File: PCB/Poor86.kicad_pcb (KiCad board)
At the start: 2 copper layers, 0 parts

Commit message: broken 386 symbol
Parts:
- added C10: 47uF, Capacitor_SMD:C_0603_1608Metric, F.Cu at (74.8, 82.2)
- added C5: 47uF, Capacitor_SMD:C_0603_1608Metric, F.Cu at (48.1, 113.2)
- added C6: 47uF, Capacitor_SMD:C_0603_1608Metric, F.Cu at (48.1, 115.7)
- added C7: 47uF, Capacitor_SMD:C_0603_1608Metric, F.Cu at (48.1, 118.2)
- added C8: 47uF, Capacitor_SMD:C_0603_1608Metric, F.Cu at (48.1, 120.7)
- added C9: 47uF, Capacitor_SMD:C_0603_1608Metric, F.Cu at (48.1, 123.2)
- added CDC1: 1uF, Capacitor_SMD:C_0402_1005Metric, F.Cu at (47.5, 97.1)
- added CDC10: 1uF, Capacitor_SMD:C_0402_1005Metric, F.Cu at (50.4, 99.1)
- added CDC11: 1uF, Capacitor_SMD:C_0402_1005Metric, F.Cu at (50.4, 101.1)
- added CDC12: 1uF, Capacitor_SMD:C_0402_1005Metric, F.Cu at (50.4, 103.0)
- added CDC13: 1uF, Capacitor_SMD:C_0402_1005Metric, F.Cu at (50.4, 105.0)
- added CDC14: 1uF, Capacitor_SMD:C_0402_1005Metric, F.Cu at (50.4, 107.0)
- added CDC15: 1uF, Capacitor_SMD:C_0402_1005Metric, F.Cu at (50.4, 109.0)
- added CDC16: 1uF, Capacitor_SMD:C_0402_1005Metric, F.Cu at (50.4, 110.9)
- added CDC17: 1uF, Capacitor_SMD:C_0402_1005Metric, F.Cu at (53.2, 97.1)
- added CDC18: 1uF, Capacitor_SMD:C_0402_1005Metric, F.Cu at (53.2, 99.1)
- added CDC19: 1uF, Capacitor_SMD:C_0402_1005Metric, F.Cu at (53.2, 101.1)
- added CDC2: 1uF, Capacitor_SMD:C_0402_1005Metric, F.Cu at (47.5, 99.1)
- added CDC20: 1uF, Capacitor_SMD:C_0402_1005Metric, F.Cu at (53.2, 103.0)
- added CDC21: 1uF, Capacitor_SMD:C_0402_1005Metric, F.Cu at (53.2, 105.0)
- added CDC22: 1uF, Capacitor_SMD:C_0402_1005Metric, F.Cu at (53.2, 107.0)
- added CDC23: 1uF, Capacitor_SMD:C_0402_1005Metric, F.Cu at (53.2, 109.0)
- added CDC24: 1uF, Capacitor_SMD:C_0402_1005Metric, F.Cu at (53.2, 110.9)
- added CDC25: 1uF, Capacitor_SMD:C_0402_1005Metric, F.Cu at (56.1, 97.1)
- added CDC26: 1uF, Capacitor_SMD:C_0402_1005Metric, F.Cu at (56.1, 99.1)
- added CDC27: 1uF, Capacitor_SMD:C_0402_1005Metric, F.Cu at (56.1, 101.1)
- added CDC28: 1uF, Capacitor_SMD:C_0402_1005Metric, F.Cu at (56.1, 103.0)
- added CDC29: 1uF, Capacitor_SMD:C_0402_1005Metric, F.Cu at (56.1, 105.0)
- added CDC3: 1uF, Capacitor_SMD:C_0402_1005Metric, F.Cu at (47.5, 101.1)
- added CDC30: 1uF, Capacitor_SMD:C_0402_1005Metric, F.Cu at (56.1, 107.0)
- added CDC31: 1uF, Capacitor_SMD:C_0402_1005Metric, F.Cu at (56.1, 109.0)
- added CDC32: 1uF, Capacitor_SMD:C_0402_1005Metric, F.Cu at (56.1, 110.9)
- added CDC33: 1uF, Capacitor_SMD:C_0402_1005Metric, F.Cu at (59.0, 97.1)
- added CDC34: 1uF, Capacitor_SMD:C_0402_1005Metric, F.Cu at (59.0, 99.1)
- added CDC35: 1uF, Capacitor_SMD:C_0402_1005Metric, F.Cu at (73.6, 58.6)
- added CDC36: 1uF, Capacitor_SMD:C_0402_1005Metric, F.Cu at (59.0, 103.0)
- added CDC37: 1uF, Capacitor_SMD:C_0402_1005Metric, F.Cu at (59.0, 105.0)
- added CDC38: 1uF, Capacitor_SMD:C_0402_1005Metric, F.Cu at (59.0, 107.0)
- added CDC4: 1uF, Capacitor_SMD:C_0402_1005Metric, F.Cu at (47.5, 103.0)
- added CDC5: 1uF, Capacitor_SMD:C_0402_1005Metric, F.Cu at (47.5, 105.0)
- added CDC6: 1uF, Capacitor_SMD:C_0402_1005Metric, F.Cu at (47.5, 107.0)
- added CDC7: 1uF, Capacitor_SMD:C_0402_1005Metric, F.Cu at (47.5, 109.0)
- added CDC8: 1uF, Capacitor_SMD:C_0402_1005Metric, F.Cu at (47.5, 110.9)
- added CDC9: 1uF, Capacitor_SMD:C_0402_1005Metric, F.Cu at (50.4, 97.1)
- added U3: ~, Package_QFP:LQFP-208_28x28mm_P0.5mm, F.Cu at (54.2, 70.1)

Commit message: ...
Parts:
- moved C6 57.6 mm to (99.2, 89.1)
- moved C7 57.6 mm to (99.2, 91.6)
- moved C8 57.6 mm to (99.2, 94.1)
- moved C9 57.6 mm to (99.2, 96.7)
- moved C5 51.6 mm to (71.4, 67.1), turned to 180 degrees
- moved C10 31.2 mm to (64.2, 52.8), turned to -90 degrees
- moved CDC35 2.92 mm to (70.8, 57.7), turned to 180 degrees
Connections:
- U3 pad 100: unconnected-(U3C-D19-Pad100) -> /am5x86/D19
- U3 pad 101: unconnected-(U3C-D18-Pad101) -> /am5x86/D18
- U3 pad 103: unconnected-(U3C-D17-Pad103) -> /am5x86/D17
- U3 pad 108: unconnected-(U3C-D16-Pad108) -> /am5x86/D16
- U3 pad 112: unconnected-(U3C-D15-Pad112) -> /am5x86/D15
- U3 pad 113: unconnected-(U3C-D14-Pad113) -> /am5x86/D14
- U3 pad 116: unconnected-(U3C-D13-Pad116) -> /am5x86/D13
- U3 pad 117: unconnected-(U3C-D12-Pad117) -> /am5x86/D12
- U3 pad 118: unconnected-(U3C-D11-Pad118) -> /am5x86/D11
- U3 pad 119: unconnected-(U3C-D10-Pad119) -> /am5x86/D10
- U3 pad 123: unconnected-(U3C-D9-Pad123) -> /am5x86/D9
- U3 pad 124: unconnected-(U3C-D8-Pad124) -> /am5x86/D8
- U3 pad 126: unconnected-(U3C-D7-Pad126) -> /am5x86/D7
- U3 pad 129: unconnected-(U3C-D6-Pad129) -> /am5x86/D6
- U3 pad 130: unconnected-(U3C-D5-Pad130) -> /am5x86/D5
- U3 pad 140: unconnected-(U3C-D4-Pad140) -> /am5x86/D4
- U3 pad 141: unconnected-(U3C-D3-Pad141) -> /am5x86/D3
- U3 pad 142: unconnected-(U3C-D2-Pad142) -> /am5x86/D2
- U3 pad 143: unconnected-(U3C-D1-Pad143) -> /am5x86/D1
- U3 pad 144: unconnected-(U3C-D0-Pad144) -> /am5x86/D0
- U3 pad 147: unconnected-(U3C-A31-Pad147) -> /am5x86/A31
- U3 pad 148: unconnected-(U3C-A30-Pad148) -> /am5x86/A30
- U3 pad 149: unconnected-(U3C-A29-Pad149) -> /am5x86/A29
- U3 pad 151: unconnected-(U3C-A28-Pad151) -> /am5x86/A28
- U3 pad 152: unconnected-(U3C-A27-Pad152) -> /am5x86/A27
- U3 pad 153: unconnected-(U3C-A26-Pad153) -> /am5x86/A26
- U3 pad 154: unconnected-(U3C-A25-Pad154) -> /am5x86/A25
- U3 pad 158: unconnected-(U3C-A24-Pad158) -> /am5x86/A24
- U3 pad 159: unconnected-(U3C-A23-Pad159) -> /am5x86/A23
- U3 pad 160: unconnected-(U3C-A22-Pad160) -> /am5x86/A22
- U3 pad 161: unconnected-(U3C-A21-Pad161) -> /am5x86/A21
- U3 pad 164: unconnected-(U3C-A20-Pad164) -> /am5x86/A20
- U3 pad 165: unconnected-(U3C-A19-Pad165) -> /am5x86/A19
- U3 pad 166: unconnected-(U3C-A18-Pad166) -> /am5x86/A18
- U3 pad 171: unconnected-(U3C-A17-Pad171) -> /am5x86/A17
- U3 pad 173: unconnected-(U3C-A16-Pad173) -> /am5x86/A16
- U3 pad 174: unconnected-(U3C-A15-Pad174) -> /am5x86/A15
- U3 pad 177: unconnected-(U3C-A14-Pad177) -> /am5x86/A14
- U3 pad 178: unconnected-(U3C-A13-Pad178) -> /am5x86/A13
- U3 pad 180: unconnected-(U3C-A12-Pad180) -> /am5x86/A12
- U3 pad 182: unconnected-(U3C-A11-Pad182) -> /am5x86/A11
- U3 pad 186: unconnected-(U3C-A10-Pad186) -> /am5x86/A10
- U3 pad 187: unconnected-(U3C-A9-Pad187) -> /am5x86/A9
- U3 pad 190: unconnected-(U3C-A8-Pad190) -> /am5x86/A8
- U3 pad 192: unconnected-(U3C-A7-Pad192) -> /am5x86/A7
- U3 pad 193: unconnected-(U3C-A6-Pad193) -> /am5x86/A6
- U3 pad 195: unconnected-(U3C-A5-Pad195) -> /am5x86/A5
- U3 pad 196: unconnected-(U3C-A4-Pad196) -> /am5x86/A4
- U3 pad 197: unconnected-(U3C-A3-Pad197) -> /am5x86/A3
- U3 pad 202: unconnected-(U3C-A2-Pad202) -> /am5x86/A2
- U3 pad 74: unconnected-(U3C-D31-Pad74) -> /am5x86/D31
- U3 pad 75: unconnected-(U3C-D30-Pad75) -> /am5x86/D30
- U3 pad 78: unconnected-(U3C-D29-Pad78) -> /am5x86/D29
- U3 pad 79: unconnected-(U3C-D28-Pad79) -> /am5x86/D28
- U3 pad 83: unconnected-(U3C-D27-Pad83) -> /am5x86/D27
- U3 pad 84: unconnected-(U3C-D26-Pad84) -> /am5x86/D26
- U3 pad 85: unconnected-(U3C-D25-Pad85) -> /am5x86/D25
- U3 pad 87: unconnected-(U3C-D24-Pad87) -> /am5x86/D24
- U3 pad 91: unconnected-(U3C-D23-Pad91) -> /am5x86/D23
- U3 pad 92: unconnected-(U3C-D22-Pad92) -> /am5x86/D22
- U3 pad 93: unconnected-(U3C-D21-Pad93) -> /am5x86/D21
- U3 pad 99: unconnected-(U3C-D20-Pad99) -> /am5x86/D20
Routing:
- net +3V3: track 0.00 -> 9.24 mm, vias 0 -> 5
- net GNDD: track 0.00 -> 2.85 mm, vias 0 -> 11
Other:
- copper layers 2 -> 4

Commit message: progress
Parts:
- added C1: 100pF, Capacitor_SMD:C_0402_1005Metric, F.Cu at (84.7, 96.4)
- added C11: 1u, Capacitor_SMD:C_0402_1005Metric, F.Cu at (99.4, 79.5)
- added C12: 1u, Capacitor_SMD:C_0402_1005Metric, F.Cu at (102.3, 71.7)
- added C13: 1u, Capacitor_SMD:C_0402_1005Metric, F.Cu at (102.3, 73.6)
- added C14: 47uF, Capacitor_SMD:C_0603_1608Metric, F.Cu at (96.0, 71.9)
- added C15: 47uF, Capacitor_SMD:C_0603_1608Metric, F.Cu at (96.0, 74.5)
- added C16: 100pF, Capacitor_SMD:C_0402_1005Metric, F.Cu at (87.5, 100.3)
- added C17: 1u, Capacitor_SMD:C_0402_1005Metric, F.Cu at (87.5, 102.3)
- added C18: 1u, Capacitor_SMD:C_0402_1005Metric, F.Cu at (87.5, 104.3)
- added C19: 1u, Capacitor_SMD:C_0402_1005Metric, F.Cu at (90.4, 96.4)
- added C2: 1u, Capacitor_SMD:C_0402_1005Metric, F.Cu at (99.4, 73.6)
- added C20: 1u, Capacitor_SMD:C_0402_1005Metric, F.Cu at (90.4, 98.3)
- added C21: 1u, Capacitor_SMD:C_0402_1005Metric, F.Cu at (90.4, 100.3)
- added C22: 1u, Capacitor_SMD:C_0402_1005Metric, F.Cu at (90.4, 102.3)
- added C23: 47uF, Capacitor_SMD:C_0603_1608Metric, F.Cu at (81.2, 101.7)
- added C24: 47uF, Capacitor_SMD:C_0603_1608Metric, F.Cu at (81.2, 104.2)
- added C3: 1u, Capacitor_SMD:C_0402_1005Metric, F.Cu at (99.4, 75.6)
- added C4: 1u, Capacitor_SMD:C_0402_1005Metric, F.Cu at (99.4, 77.6)
- added L1: 2.2uH, Inductor_SMD:L_1008_2520Metric, F.Cu at (113.3, 79.7)
- added L2: 2.2uH, Inductor_SMD:L_1008_2520Metric, F.Cu at (85.7, 110.9)
- added R1: 15k, Resistor_SMD:R_0402_1005Metric, F.Cu at (93.3, 96.4)
- added R2: 18k, Resistor_SMD:R_0402_1005Metric, F.Cu at (93.3, 98.4)
- added R3: 15k, Resistor_SMD:R_0402_1005Metric, F.Cu at (93.3, 100.4)
- added R4: 4.7K, Resistor_SMD:R_0402_1005Metric, F.Cu at (93.3, 102.4)
- added U1: LFE5U-25F-6BG256C, ECP5:BGA256C80P16X16_1400X1400X170, F.Cu at (51.2, 109.6)
- added U2: TLV62569DBV, Package_TO_SOT_SMD:SOT-23-5, F.Cu at (111.7, 86.3)
- added U4: TLV62569DBV, Package_TO_SOT_SMD:SOT-23-5, F.Cu at (73.5, 104.3)
- added U5: TLV62569DBV, Package_TO_SOT_SMD:SOT-23-5, F.Cu at (73.5, 108.9)
- CDC1, CDC10, CDC11, CDC12, CDC13, CDC14, CDC15, CDC16, CDC17, CDC18, CDC19, CDC2, CDC20, CDC21, CDC22, CDC23, CDC24, CDC25, CDC26, CDC27, CDC28, CDC29, CDC3, CDC30, CDC31, CDC32, CDC33, CDC34, CDC36, CDC37, CDC38, CDC4, CDC5, CDC6, CDC7, CDC8, CDC9: moved to B.Cu
- moved C8 68.0 mm to (37.0, 66.6)
- moved C6 65.7 mm to (37.0, 68.2)
- moved C9 64.7 mm to (37.0, 79.1)
- moved CDC16 46.5 mm to (52.2, 64.5)
- moved CDC24 46.5 mm to (55.0, 64.5)
- moved CDC32 46.5 mm to (57.9, 64.5)
- moved CDC8 46.5 mm to (49.3, 64.5)
- moved CDC15 42.5 mm to (52.2, 66.5)
- moved CDC23 42.5 mm to (55.0, 66.5)
- moved CDC31 42.5 mm to (57.9, 66.5)
- moved CDC7 42.5 mm to (49.3, 66.5)
- moved CDC14 38.6 mm to (52.2, 68.4)
- moved CDC22 38.6 mm to (55.0, 68.4)
- moved CDC30 38.6 mm to (57.9, 68.4)
- moved CDC6 38.6 mm to (49.3, 68.4)
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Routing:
- net GNDD: track 2.85 -> 20.3 mm, vias 11 -> 38
- net +3V3: track 9.24 -> 24.1 mm, vias 5 -> 13
- net VCCIO7: vias 0 -> 2
- net VCCIO6: vias 0 -> 2
- net VCCIO3: vias 0 -> 2
- net VCCIO2: vias 0 -> 2
- net VCCIO1: vias 0 -> 2
- net VCCIO0: vias 0 -> 2
- net +2V5: vias 0 -> 2
- net +1V1: vias 0 -> 6
- added copper zone on In2.Cu, net +1V1
- added copper zone on In1.Cu, net GNDD

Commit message: more progress
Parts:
- added C25: 100pF, Capacitor_SMD:C_0402_1005Metric, F.Cu at (17.0, 148.3)
- added C26: 1u, Capacitor_SMD:C_0402_1005Metric, F.Cu at (21.5, 148.3)
- added C27: 1u, Capacitor_SMD:C_0402_1005Metric, F.Cu at (26.0, 148.3)
- added C28: 1u, Capacitor_SMD:C_0402_1005Metric, F.Cu at (30.5, 148.3)
- added C29: 1u, Capacitor_SMD:C_0402_1005Metric, F.Cu at (35.0, 148.3)
- added C30: 1u, Capacitor_SMD:C_0402_1005Metric, F.Cu at (37.2, 148.3)
- added C31: 1u, Capacitor_SMD:C_0402_1005Metric, F.Cu at (41.7, 148.3)
- added C32: 47uF, Capacitor_SMD:C_0603_1608Metric, F.Cu at (39.5, 148.3)
- added C33: 47uF, Capacitor_SMD:C_0603_1608Metric, F.Cu at (44.0, 148.3)
- added D1: 1N4001, Diode_SMD:D_0402_1005Metric, F.Cu at (22.8, 23.2)
- added J1: Bus_ISA_8bit, Connector_PinHeader_2.54mm:PinHeader_2x31_P2.54mm_Vertical_SMD, F.Cu at (63.6, 174.5)
- added J2: 7-5530843-0, ISA:TE_7-5530843-0, F.Cu at (61.6, 159.6)
- added J3: ATX-20, Connector_Molex:Molex_Mini-Fit_Jr_5566-20A_2x10_P4.20mm_Vertical, F.Cu at (57.0, 14.8)
- added JP1: Closed=3.3V, Open=3.5V, Jumper:SolderJumper-2_P1.3mm_Bridged_Pad1.0x1.5mm, F.Cu at (48.5, 148.3)
- added L3: 2.2uH, Inductor_SMD:L_1008_2520Metric, F.Cu at (46.2, 148.3)
- added P1: USB_C_Plug_USB2.0, Connector_USB:USB_C_Receptacle_GCT_USB4105-xx-A_16P_TopMnt_Horizontal, F.Cu at (16.0, 18.0)
- added R5: 15k, Resistor_SMD:R_0402_1005Metric, F.Cu at (19.2, 148.3)
- added R6: 3.3k, Resistor_SMD:R_0402_1005Metric, F.Cu at (23.7, 148.3)
- added R7: 1k, Resistor_SMD:R_0402_1005Metric, F.Cu at (28.2, 148.3)
- added SW3: SW_Push_Dual, Button_Switch_THT:SW_PUSH_6mm, F.Cu at (100.5, 18.9)
- added SW4: SW_Push_Dual, Button_Switch_THT:SW_PUSH_6mm, F.Cu at (100.5, 27.5)
- added U10: IS66WVE4M16EBLL-70BLI, ISSI:TFBGA48_ISI, F.Cu at (50.4, 55.6)
- added U11: CH552T, Package_SO:TSSOP-20-1EP_4.4x6.5mm_P0.65mm_EP2.15x3.35mm, F.Cu at (25.6, 18.6)
- added U6: TLV62569DBV, Package_TO_SOT_SMD:SOT-23-5, F.Cu at (32.8, 148.3)
- added U9: IS66WVE4M16EBLL-70BLI, ISSI:TFBGA48_ISI, F.Cu at (50.2, 68.9)
- C15, C24: value 47uF -> 10uF
- U3: value ~ -> AM5x86 PQFP208
- U5: value TLV62569DBV -> ESP-12F; footprint Package_TO_SOT_SMD:SOT-23-5 -> RF_Module:ESP-12E
- moved C12 92.4 mm to (50.7, 148.3), turned to 90 degrees
- moved C14 87.6 mm to (53.0, 148.3), turned to 90 degrees
- moved C13 87.1 mm to (57.5, 148.3), turned to 90 degrees
- moved C2 86.8 mm to (55.2, 148.3), turned to 90 degrees
- moved C15 82.3 mm to (59.7, 148.3), turned to 90 degrees
- moved L1 81.9 mm to (68.7, 148.3), turned to 90 degrees
- moved C3 81.8 mm to (62.0, 148.3), turned to 90 degrees
- moved C4 79.0 mm to (64.2, 148.3), turned to 90 degrees
- moved C11 76.2 mm to (66.5, 148.3), turned to 90 degrees
- moved U2 74.1 mm to (71.0, 148.3), turned to 90 degrees
- moved U5 59.7 mm to (16.5, 126.4), turned to 90 degrees
- moved C19 54.7 mm to (73.2, 148.3), turned to 90 degrees
- moved R1 54.2 mm to (77.7, 148.3), turned to 90 degrees
- moved C1 52.7 mm to (75.4, 148.3), turned to 90 degrees
- moved U4 52.7 mm to (102.5, 148.3), turned to 90 degrees
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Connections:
- U1 pad M10: unconnected-(U1H-TDO-PadM10) -> TDO
- U1 pad R11: unconnected-(U1H-TDI-PadR11) -> TDI
- U1 pad T10: unconnected-(U1H-TCK-PadT10) -> TCK
- U1 pad T11: unconnected-(U1H-TMS-PadT11) -> TMS
- U2 pad 1: +3V3 -> +5V
- U2 pad 4: +3V3 -> +5V
- U4 pad 1: +3V3 -> +5V
- U4 pad 4: +3V3 -> +5V
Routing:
- net Net-(U11-VBUS): track 0.00 -> 3.25 mm
- net Net-(P1-D+): track 0.00 -> 3.11 mm
- net Net-(P1-D-): track 0.00 -> 3.07 mm
- net Net-(D1-K): track 0.00 -> 1.25 mm
- net GNDD: track 20.3 -> 21.2 mm, vias 38 -> 12
- net +3V3: track 24.1 -> 24.6 mm, vias 13 -> 14
- net VCCIO7: vias 2 -> 0
- net VCCIO6: vias 2 -> 0
- net VCCIO3: vias 2 -> 0
- net VCCIO2: vias 2 -> 0
- net VCCIO1: vias 2 -> 0
- net VCCIO0: vias 2 -> 0
- net +2V5: vias 2 -> 0
- net +1V1: vias 6 -> 0
- removed copper zone on In2.Cu, net +1V1
- removed copper zone on In1.Cu, net GNDD
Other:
- board outline added: 100 x 170 mm

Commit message: more progress
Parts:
- removed J2: 7-5530843-0, ISA:TE_7-5530843-0
- removed U10, U9: IS66WVE4M16EBLL-70BLI, ISSI:TFBGA48_ISI
- added U12: IS66WVH8M8BLL-100B1LI, Package_BGA:BGA-24_6x8mm_Layout5x5_P1.0mm, F.Cu at (39.0, 123.0)
- added U13: IS66WVH8M8BLL-100B1LI, Package_BGA:BGA-24_6x8mm_Layout5x5_P1.0mm, F.Cu at (39.0, 115.0)
- added U14: KM416x254, Package_SO:TSOP-II-40-44_10.16x18.37mm_P0.8mm, F.Cu at (76.0, 37.0)
- added U15: KM416x254, Package_SO:TSOP-II-40-44_10.16x18.37mm_P0.8mm, F.Cu at (56.0, 37.0)
- added U7: RP2354B, Package_DFN_QFN:QFN-80-1EP_10x10mm_P0.4mm_EP3.4x3.4mm, F.Cu at (53.0, 102.7)
- D1: footprint Diode_SMD:D_0402_1005Metric -> Diode_SMD:D_1206_3216Metric_Pad1.42x1.75mm_HandSolder
- J1: footprint Connector_PinHeader_2.54mm:PinHeader_2x31_P2.54mm_Vertical_SMD -> ISA:TE_7-5530843-0
- moved D1 117.8 mm to (22.3, 141.0)
- moved P1 116.3 mm to (15.5, 134.2)
- moved U11 116.3 mm to (25.1, 134.8)
- moved C8 74.1 mm to (79.5, 136.2), turned to 90 degrees
- moved C6 73.0 mm to (81.0, 136.2), turned to 90 degrees
- moved C9 65.8 mm to (92.0, 136.2), turned to 90 degrees
- moved C10 65.5 mm to (65.8, 109.0), turned to 0 degrees
- moved J3 59.4 mm to (101.5, 54.0), turned to 90 degrees
- moved CDC35 56.3 mm to (70.6, 102.4), turned to -90 degrees
- moved SW3 56.0 mm to (107.0, 74.5), turned to 180 degrees
- moved U3 52.3 mm to (83.0, 119.0), turned to 90 degrees
- moved CDC16 51.0 mm to (81.7, 112.2)
- moved CDC24 51.0 mm to (84.6, 112.2)
- moved CDC32 51.0 mm to (87.5, 112.2)
- moved CDC8 51.0 mm to (78.9, 112.2)
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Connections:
- U1 pad M10: TDO -> Net-(U1H-TDO)
- U3 pad 167: unconnected-(U3B-TMS-Pad167) -> TMS
- U3 pad 168: unconnected-(U3B-TDI-Pad168) -> Net-(U1H-TDO)
- U3 pad 18: unconnected-(U3B-TCK-Pad18) -> TCK
- U3 pad 68: unconnected-(U3B-TDO-Pad68) -> TDO
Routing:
- net Net-(D1-K): track 1.25 -> 1.82 mm
- net +3V3: track 24.6 -> 24.1 mm, vias 14 -> 13

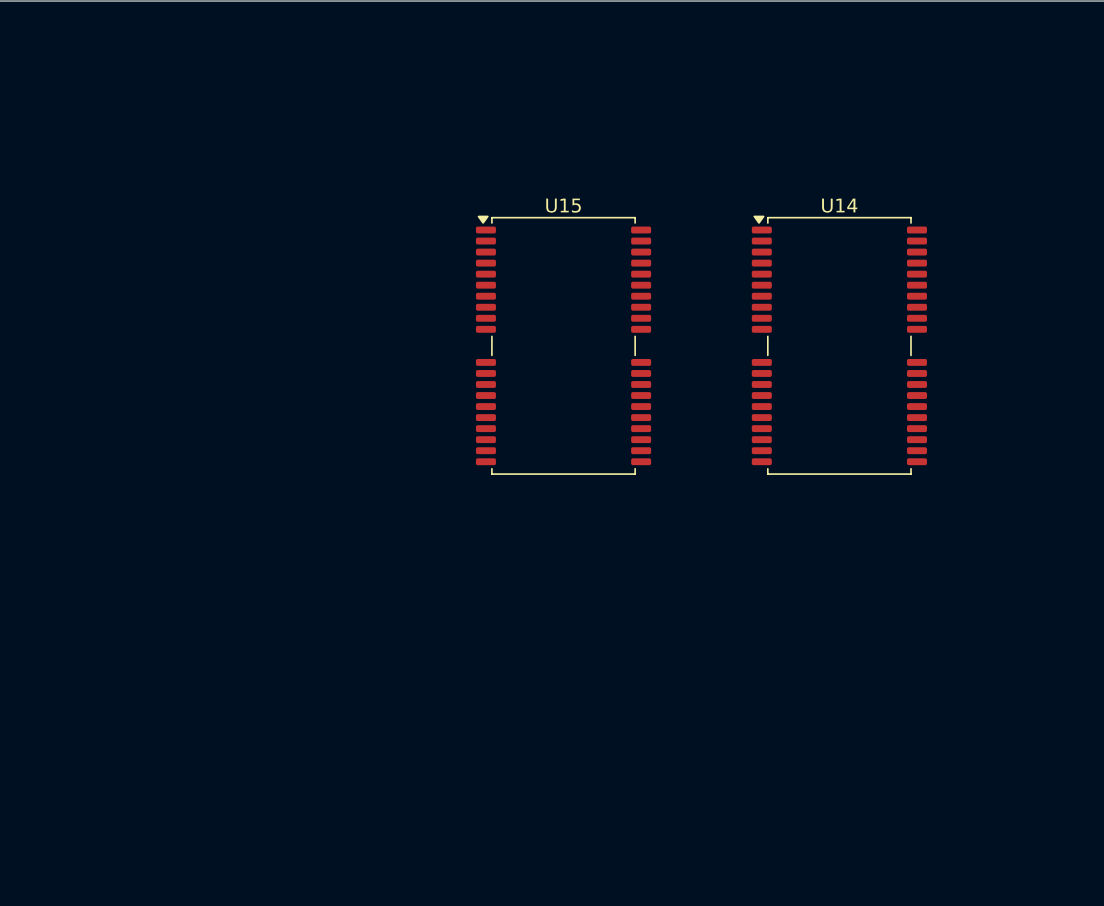
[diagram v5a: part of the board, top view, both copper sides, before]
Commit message: adding video chip and support bits
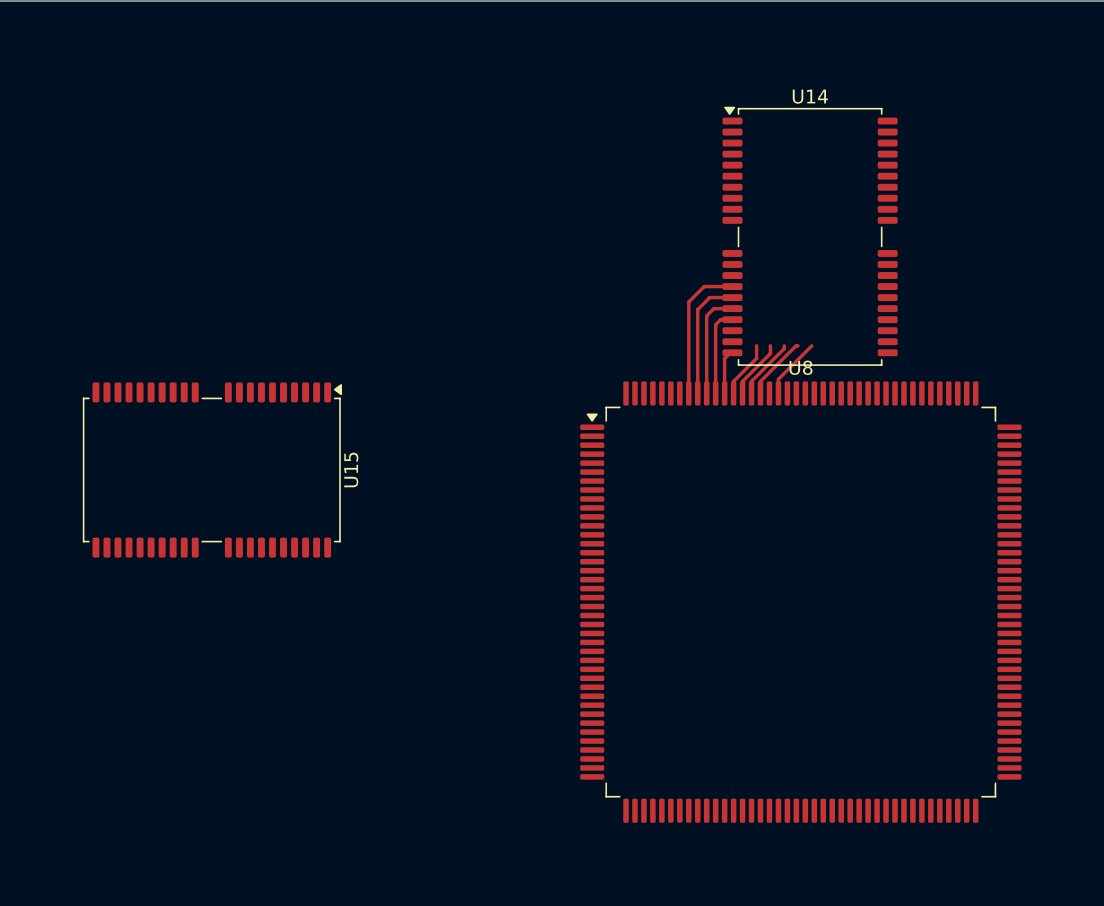
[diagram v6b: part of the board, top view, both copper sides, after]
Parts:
- added U8: CL-GD5428-LOCALBUS, Package_QFP:PQFP-160_28x28mm_P0.65mm, F.Cu at (73.2, 55.6)
- moved U15 27.0 mm to (30.5, 46.0), turned to -90 degrees
- moved U14 8.18 mm to (73.9, 29.1)
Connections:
- U14 pad 16: unconnected-(U14-A0-Pad16) -> /VideoSubSystem/MA0
- U14 pad 17: unconnected-(U14-A1-Pad17) -> /VideoSubSystem/MA1
- U14 pad 18: unconnected-(U14-A2-Pad18) -> /VideoSubSystem/MA2
- U14 pad 19: unconnected-(U14-A3-Pad19) -> /VideoSubSystem/MA3
- U14 pad 22: unconnected-(U14-A4-Pad22) -> /VideoSubSystem/MA4
- U14 pad 23: unconnected-(U14-A5-Pad23) -> /VideoSubSystem/MA5
- U14 pad 24: unconnected-(U14-A6-Pad24) -> /VideoSubSystem/MA6
- U14 pad 25: unconnected-(U14-A7-Pad25) -> /VideoSubSystem/MA7
- U14 pad 26: unconnected-(U14-A8-Pad26) -> /VideoSubSystem/MA8
- U14 pad 28: unconnected-(U14-~{UCAS}-Pad28) -> Net-(U14-~{LCAS})
- U14 pad 29: unconnected-(U14-~{LCAS}-Pad29) -> Net-(U14-~{LCAS})
- U15 pad 16: unconnected-(U15-A0-Pad16) -> /VideoSubSystem/MA0
- U15 pad 17: unconnected-(U15-A1-Pad17) -> /VideoSubSystem/MA1
- U15 pad 18: unconnected-(U15-A2-Pad18) -> /VideoSubSystem/MA2
- U15 pad 19: unconnected-(U15-A3-Pad19) -> /VideoSubSystem/MA3
- U15 pad 22: unconnected-(U15-A4-Pad22) -> /VideoSubSystem/MA4
- U15 pad 23: unconnected-(U15-A5-Pad23) -> /VideoSubSystem/MA5
- U15 pad 24: unconnected-(U15-A6-Pad24) -> /VideoSubSystem/MA6
- U15 pad 25: unconnected-(U15-A7-Pad25) -> /VideoSubSystem/MA7
- U15 pad 26: unconnected-(U15-A8-Pad26) -> /VideoSubSystem/MA8
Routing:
- net /VideoSubSystem/MA0: track 0.00 -> 10.3 mm
- net /VideoSubSystem/MA1: track 0.00 -> 8.96 mm
- net /VideoSubSystem/MA2: track 0.00 -> 7.72 mm
- net /VideoSubSystem/MA3: track 0.00 -> 6.35 mm
- net /VideoSubSystem/MA8: track 0.00 -> 4.66 mm
- net /VideoSubSystem/MA9: track 0.00 -> 4.45 mm
- net /VideoSubSystem/MA7: track 0.00 -> 4.43 mm
- net /VideoSubSystem/MA6: track 0.00 -> 4.29 mm
- net /VideoSubSystem/MA5: track 0.00 -> 4.14 mm
- net /VideoSubSystem/MA4: track 0.00 -> 3.27 mm
